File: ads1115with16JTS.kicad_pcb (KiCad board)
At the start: 2 copper layers, 45.7 x 68.5 mm, 52 parts, among them J1 Conn_01x02_Pin, J10 Conn_01x02_Pin, J11 Conn_01x02_Pin, J12 Conn_01x02_Pin, J13 Conn_01x02_Pin, J14 Conn_01x02_Pin, J15 Conn_01x02_Pin, J16 Conn_01x02_Pin, J17 Conn_01x04_Pin, J18 PinSocket_1x20_P2.54mm_Vertic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, J19 PinSocket_1x20_P2.54mm_Vertic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, J2 Conn_01x02_Pin, J20 Screw_Terminal_01x02, J3 Conn_01x02_Pin, J4 Conn_01x02_Pin, J5 Conn_01x02_Pin, J6 Conn_01x02_Pin, J7 Conn_01x02_Pin, J8 Conn_01x02_Pin, J9 Conn_01x02_Pin, U1 ADS1115IDGS, U2 ADS1115IDGS, U3 ADS1115IDGS, U4 ADS1115IDGS

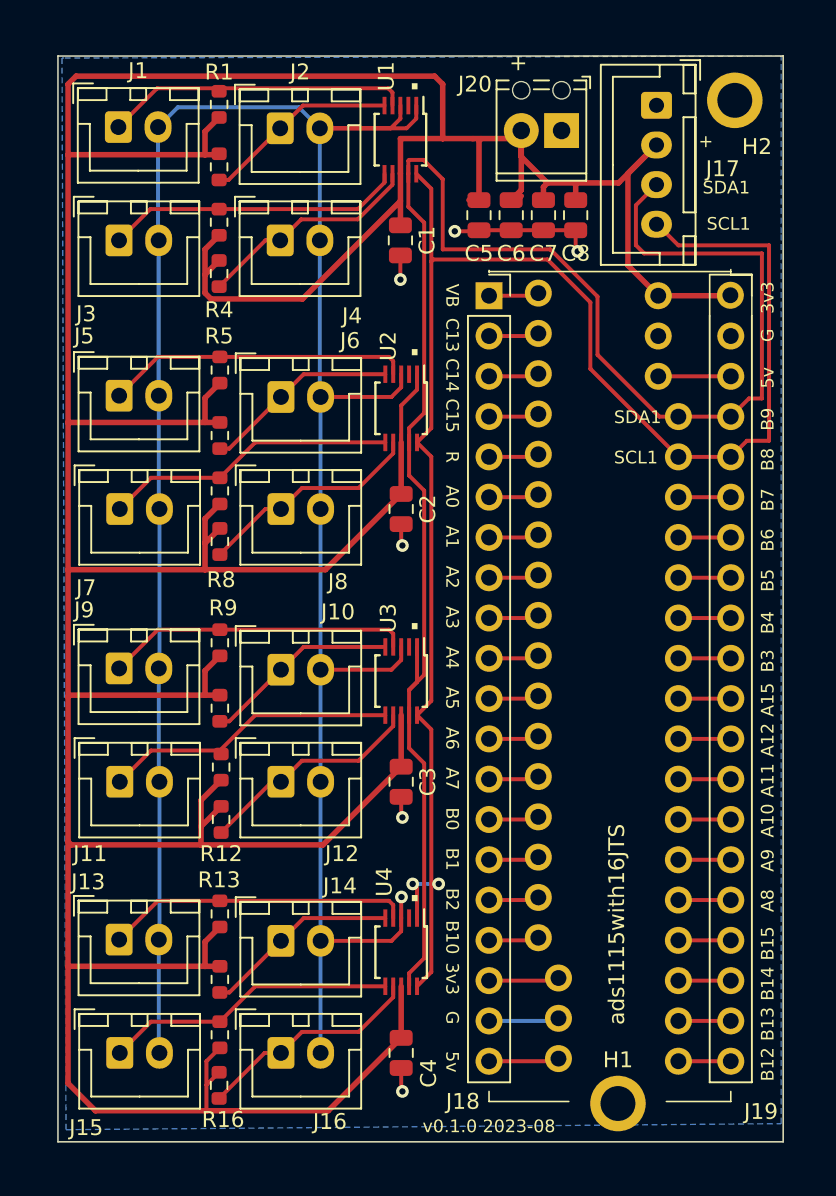
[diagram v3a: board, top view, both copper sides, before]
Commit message: sized slightly larger, added 2 more mounting holes.
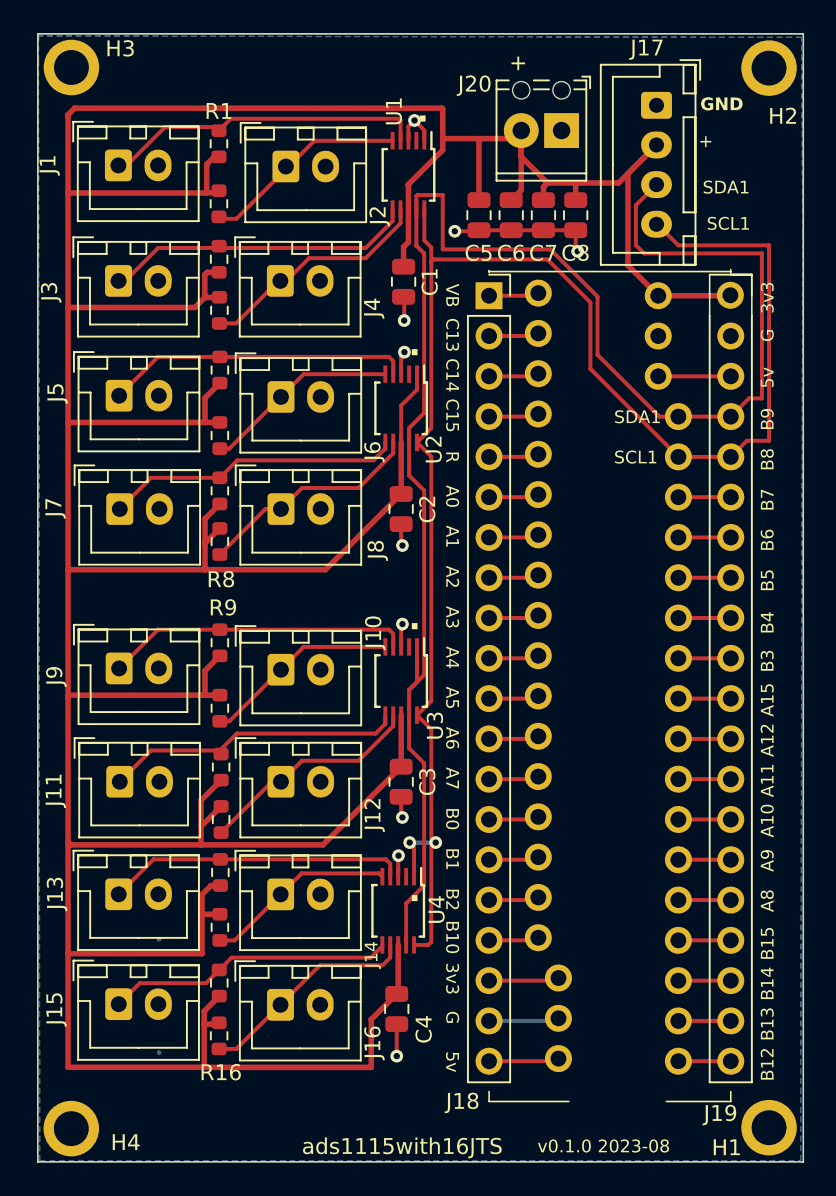
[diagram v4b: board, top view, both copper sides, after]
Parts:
- added H3: MountingHole, ProjectLib:MountingHole_2.2mm_M2_ISO7380_Pad, F.Cu at (51.6, 26.2)
- added H4: MountingHole, ProjectLib:MountingHole_2.2mm_M2_ISO7380_Pad, F.Cu at (51.6, 93.2)
- moved H1 9.65 mm to (95.6, 93.1)
- moved R14 3.28 mm to (61.0, 80.5)
- moved R15 3.26 mm to (61.0, 84.0)
- moved R16 3.12 mm to (61.0, 87.3)
- moved J15 3.07 mm to (54.6, 85.3)
- moved J16 3.03 mm to (64.8, 85.3)
- moved H2 2.96 mm to (95.6, 26.3)
- moved J14 2.93 mm to (64.8, 78.4)
- moved J13 2.86 mm to (54.6, 78.4)
- moved C4 2.78 mm to (72.2, 85.6)
- moved C1 2.62 mm to (72.6, 39.8)
- moved U4 2.61 mm to (72.2, 79.4)
- moved R13 2.61 mm to (61.0, 77.0)
- moved J3 2.56 mm to (54.6, 39.7)
- moved J4 2.56 mm to (64.8, 39.7)
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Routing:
- net GND: track 180.5 -> 27.2 mm, vias 7 -> 10
- net +3V3: track 314.6 -> 305.5 mm
- net /SDA1: track 112.3 -> 105.3 mm
- net /SCL1: track 106.7 -> 101.8 mm
- net Net-(J4-Pin_1): track 14.3 -> 15.9 mm
- net Net-(J1-Pin_1): track 19.2 -> 20.0 mm
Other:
- board size 45.7 x 68.5 mm -> 48.3 x 71.1 mm
- board text added: "GND"

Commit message: Footprint adjustments to get tthem all from ProjectLib.pretty. Using Kicad 8.0.1.
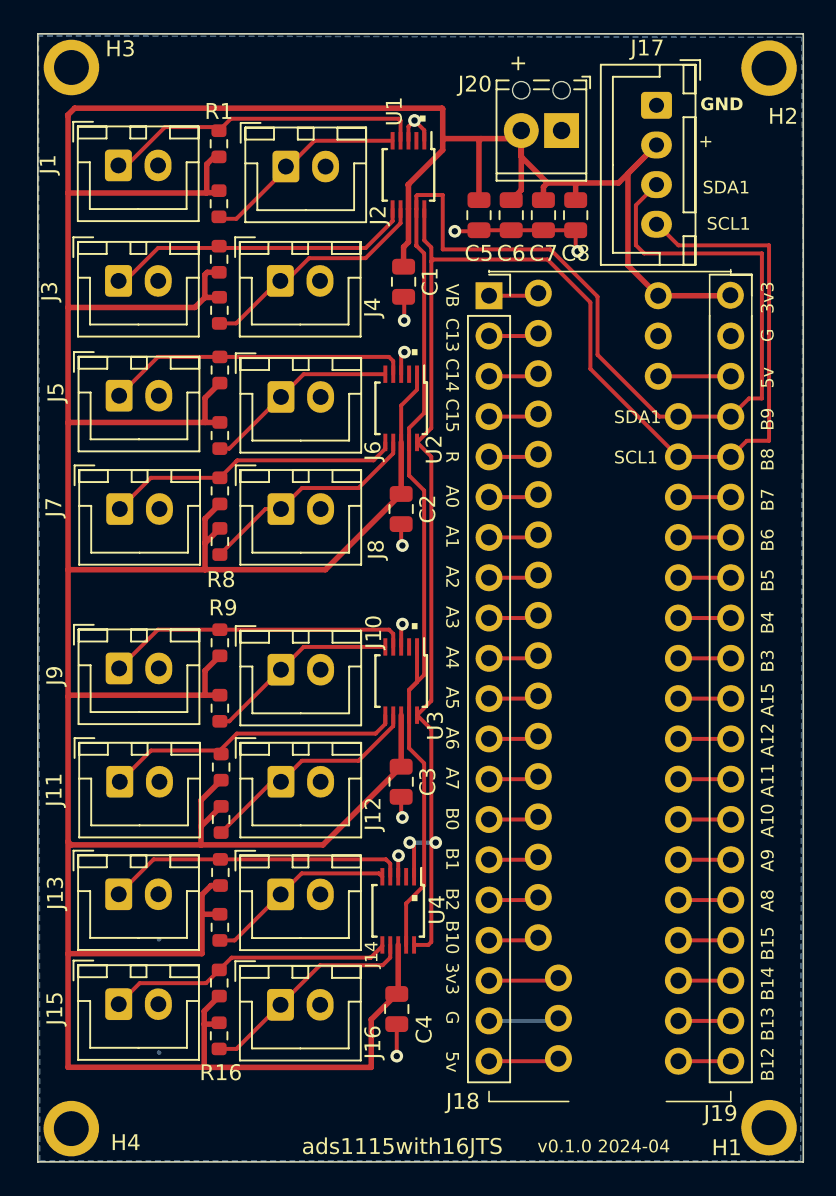
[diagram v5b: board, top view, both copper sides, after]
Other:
- board text added: "v0.1.0 2024-04"
- board text removed: "v0.1.0 2023-08"

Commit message: Removed test points because there is no room. Trying to sync symbol footprints and pcb footprints.
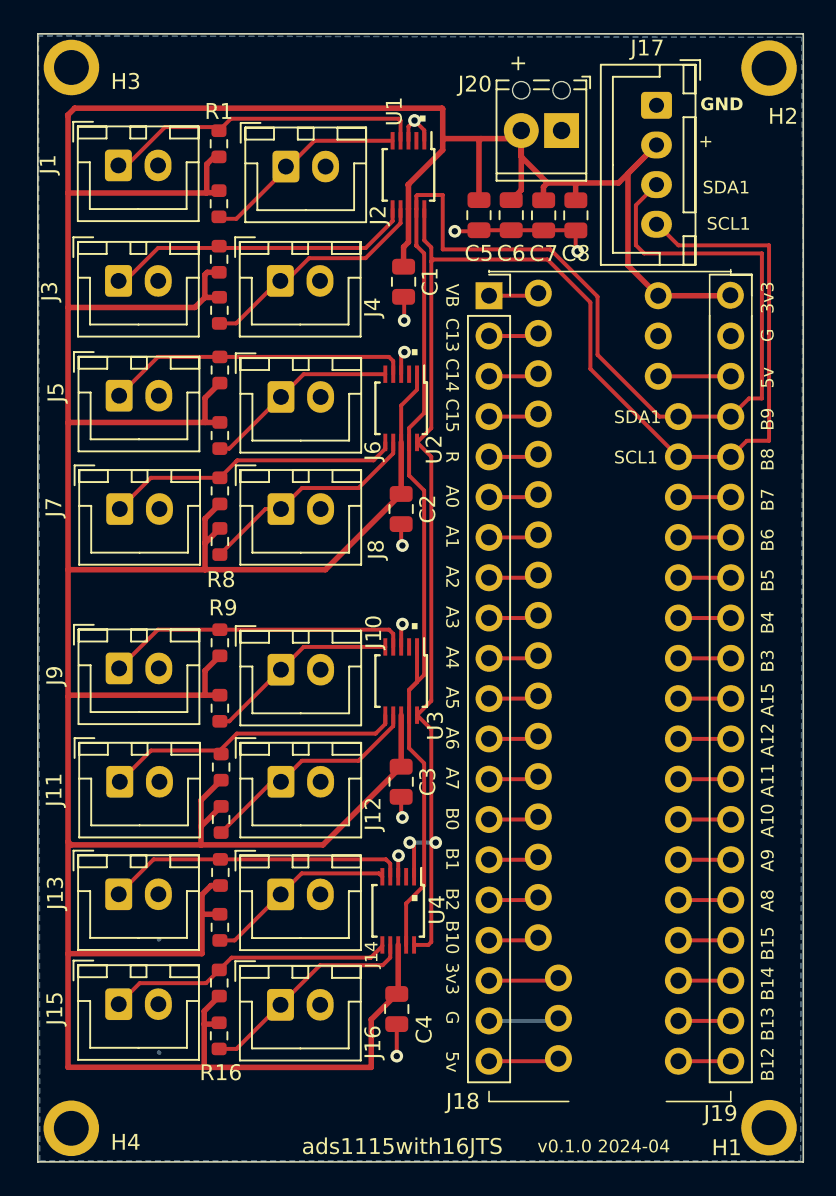
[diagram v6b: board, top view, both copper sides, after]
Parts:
- C1, C2, C3, C4: value 0.1µF1 -> 0.1µF
- C5, C7: value 10µF5 -> 10µF
- C6, C8: value 10µF6 -> 10µF

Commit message: DRC runs clean.
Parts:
- removed the C5 at (77.3, 35.6)
- removed the C6 at (79.4, 35.6)
- added C7: 10µF, ProjectLib:C_0805_2012Metric, F.Cu at (79.4, 35.6)
- added C8: 10µF, ProjectLib:C_0805_2012Metric, F.Cu at (77.3, 35.6)
- renumbered C8 to C5, C7 to C6

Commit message: as first submit to PCBway.
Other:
- board text added: "v0.1.0 2024-05"
- board text removed: "v0.1.0 2024-04"
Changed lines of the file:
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@@
 		(pad_to_mask_clearance 0)
 		(allow_soldermask_bridges_in_footprints no)
-		(aux_axis_origin 49.53 95.25)
+		(aux_axis_origin 49.65 95.19)
+		(grid_origin 49.65 95.19)
 		(pcbplotparams
 			(layerselection 0x00310fc_ffffffff)
@@
 		)
 	)
-	(gr_text "v0.1.0 2024-04"
+	(gr_text "v0.1.0 2024-05"
 		(at 81.026 94.742 0)
 		(layer "F.SilkS")
